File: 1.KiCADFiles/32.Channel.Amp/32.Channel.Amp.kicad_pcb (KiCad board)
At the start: 2 copper layers, 150 x 170.5 mm, 35 parts

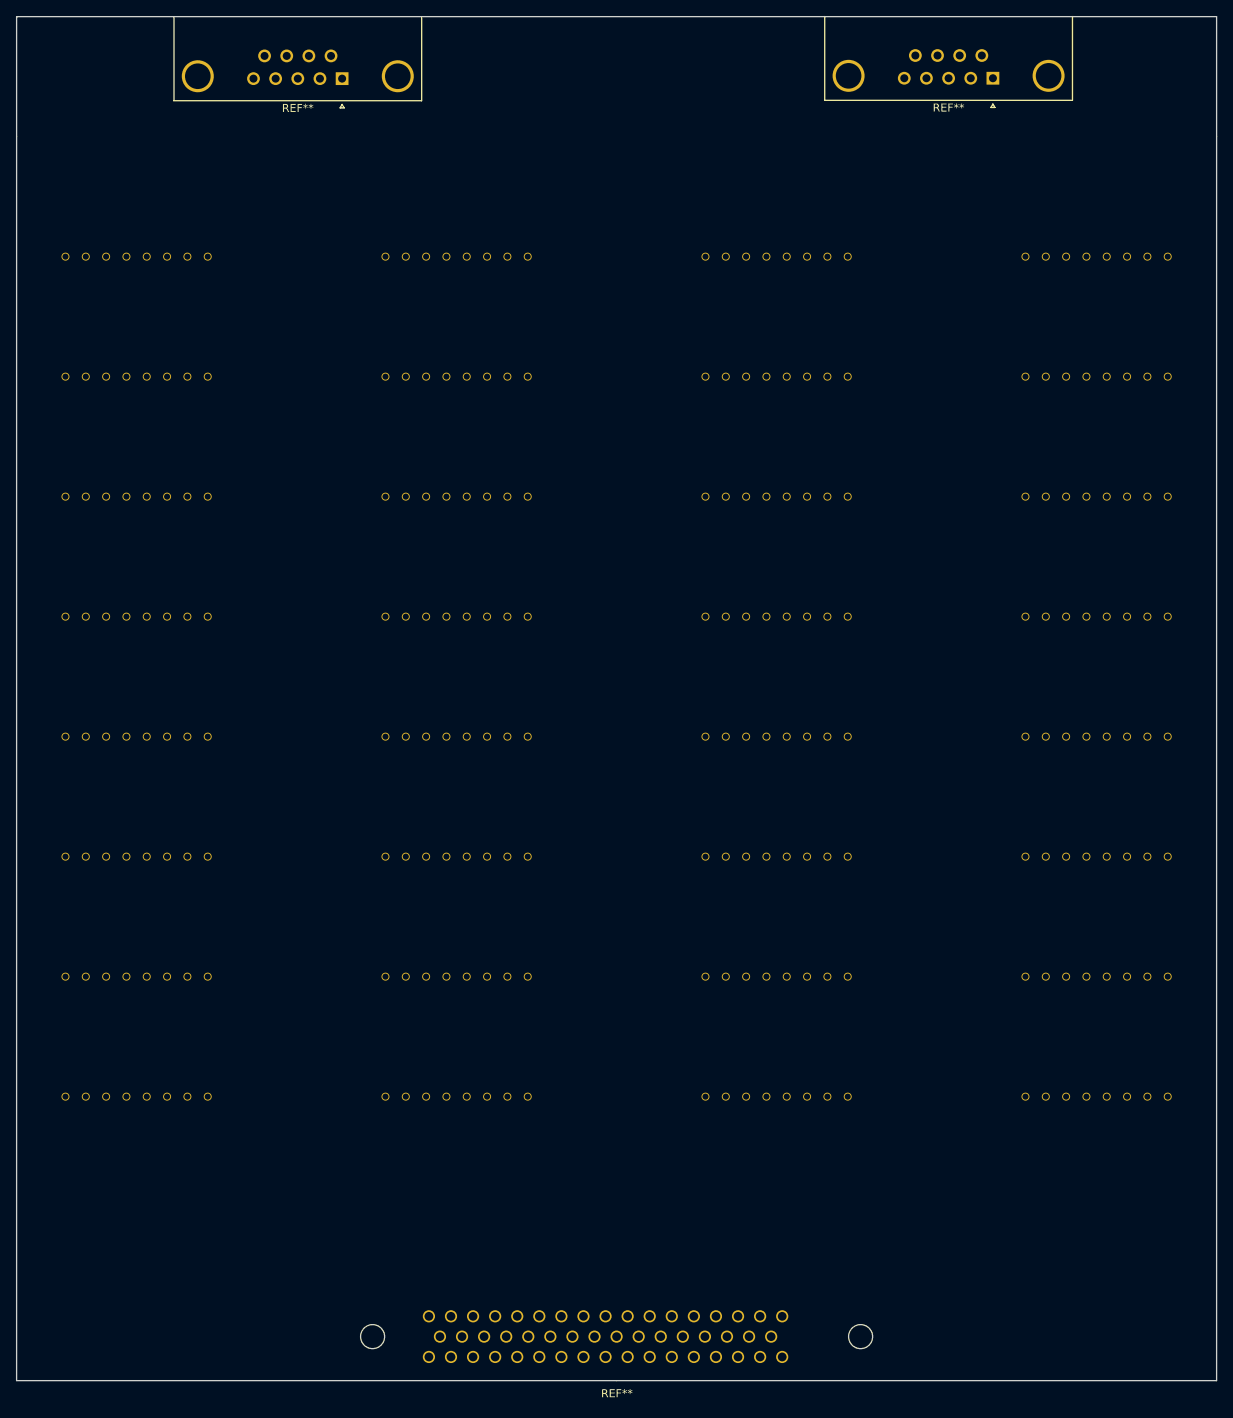
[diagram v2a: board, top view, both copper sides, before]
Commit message: Added +V and -V regulators
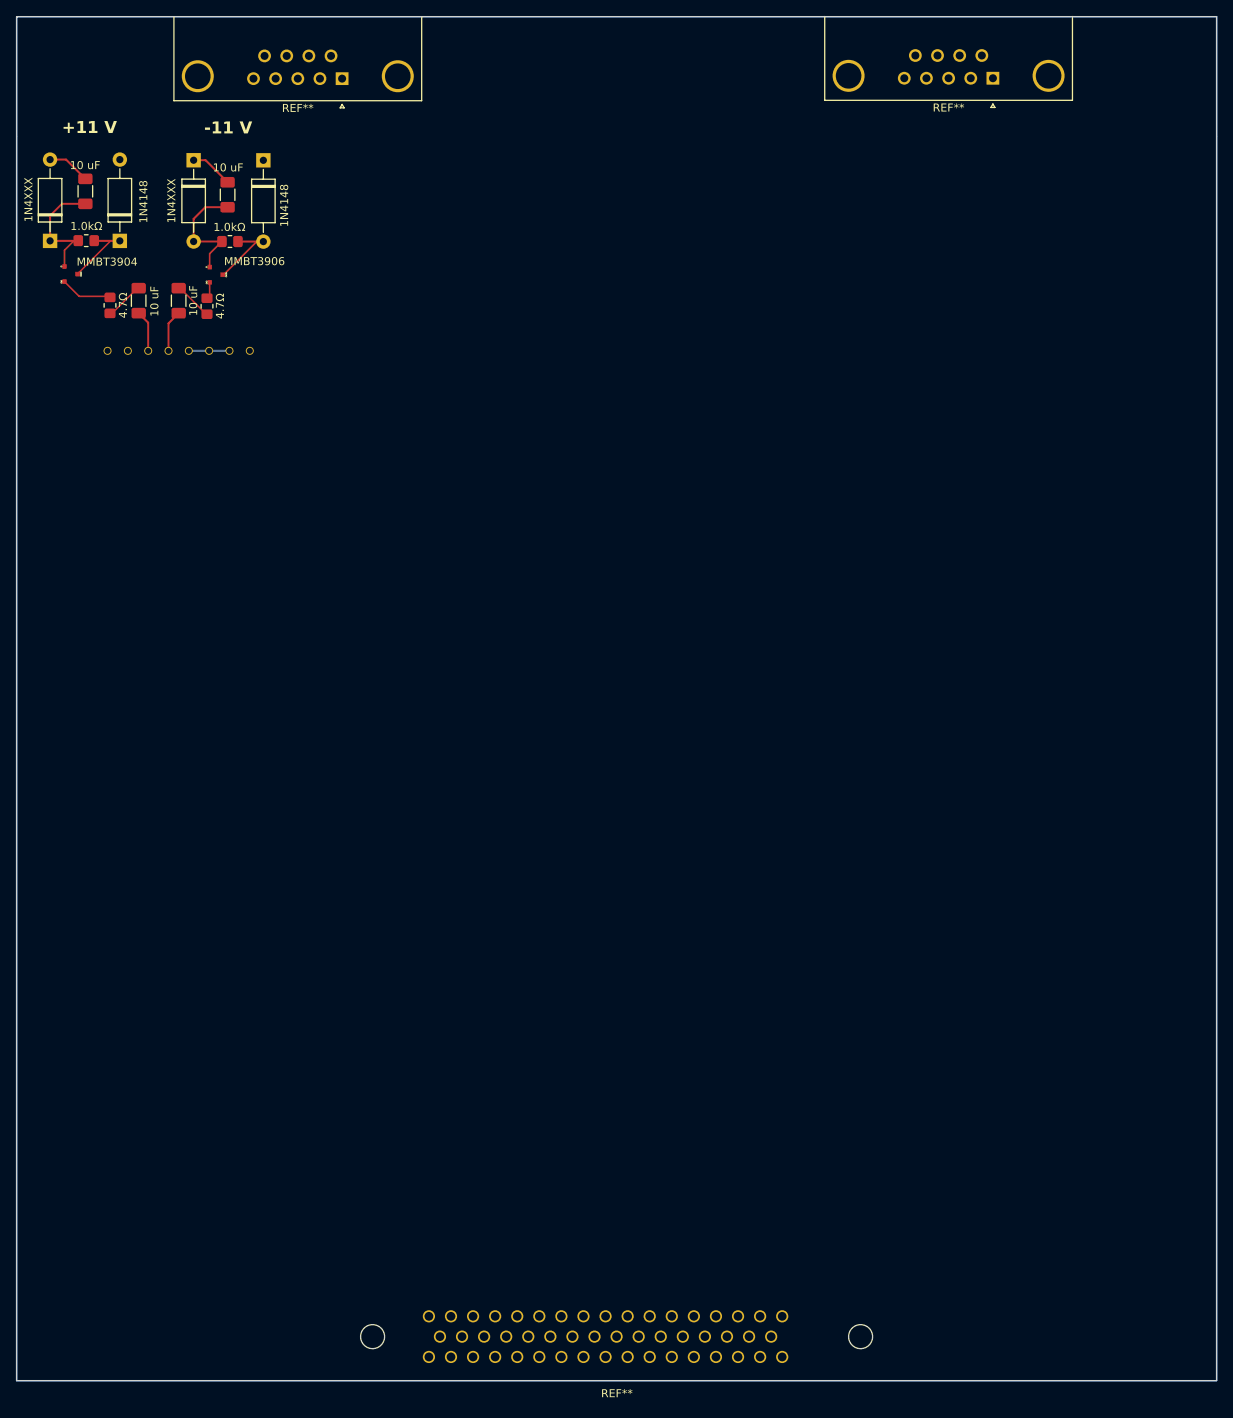
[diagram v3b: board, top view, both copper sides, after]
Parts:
- removed REF**1, REF**10, REF**11, REF**12, REF**13, REF**14, REF**15, REF**16, REF**17, REF**18, REF**19, REF**2, REF**20, REF**21, REF**22, REF**23, REF**24, REF**25, REF**26, REF**27, REF**28, REF**29, REF**3, REF**30, REF**31, REF**4, REF**5, REF**6, REF**7, REF**8, REF**9: SMC-1-08-1-GT, 1.Local.Library:SMC-1-08-1-GT
- added 1.0kΩ: R_0805_2012Metric_Pad1.20x1.40mm_HandSolder, Resistor_SMD:R_0805_2012Metric_Pad1.20x1.40mm_HandSolder, F.Cu at (56.7, 28.1)
- added 1.0kΩ: R_0805_2012Metric_Pad1.20x1.40mm_HandSolder, Resistor_SMD:R_0805_2012Metric_Pad1.20x1.40mm_HandSolder, F.Cu at (38.7, 28.0)
- added 10 uF: C_1206_3216Metric_Pad1.33x1.80mm_HandSolder, Capacitor_SMD:C_1206_3216Metric_Pad1.33x1.80mm_HandSolder, F.Cu at (45.3, 35.5)
- added 10 uF: C_1206_3216Metric_Pad1.33x1.80mm_HandSolder, Capacitor_SMD:C_1206_3216Metric_Pad1.33x1.80mm_HandSolder, F.Cu at (56.4, 22.3)
- added 10 uF: C_1206_3216Metric_Pad1.33x1.80mm_HandSolder, Capacitor_SMD:C_1206_3216Metric_Pad1.33x1.80mm_HandSolder, F.Cu at (50.3, 35.5)
- added 10 uF: C_1206_3216Metric_Pad1.33x1.80mm_HandSolder, Capacitor_SMD:C_1206_3216Metric_Pad1.33x1.80mm_HandSolder, F.Cu at (38.6, 21.8)
- added 1N4148: D_A-405_P10.16mm_Horizontal, Diode_THT:D_A-405_P10.16mm_Horizontal, F.Cu at (60.8, 18.0)
- added 1N4148: D_A-405_P10.16mm_Horizontal, Diode_THT:D_A-405_P10.16mm_Horizontal, F.Cu at (42.9, 28.0)
- added 1N4XXX: D_A-405_P10.16mm_Horizontal, Diode_THT:D_A-405_P10.16mm_Horizontal, F.Cu at (52.1, 17.9)
- added 1N4XXX: D_A-405_P10.16mm_Horizontal, Diode_THT:D_A-405_P10.16mm_Horizontal, F.Cu at (34.2, 28.0)
- added 4.7Ω: R_0805_2012Metric_Pad1.20x1.40mm_HandSolder, Resistor_SMD:R_0805_2012Metric_Pad1.20x1.40mm_HandSolder, F.Cu at (53.8, 36.2)
- added 4.7Ω: R_0805_2012Metric_Pad1.20x1.40mm_HandSolder, Resistor_SMD:R_0805_2012Metric_Pad1.20x1.40mm_HandSolder, F.Cu at (41.7, 36.1)
- added MMBT3904: MMBT3904, 1.Local.Library:MMBT3904, F.Cu at (36.2, 32.2)
- added MMBT3906: MMBT3906, 1.Local.Library:MMBT3906, F.Cu at (54.4, 32.3)
- moved REF** 12.9 mm to (50.3, 41.8), turned to 180 degrees
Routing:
- net (no net): track 0.00 -> 55.8 mm
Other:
- board text added: "+11 V"
- board text added: "-11 V"

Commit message: Added Power Regulator, RC Filtering, and 32 Channel
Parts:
- removed the REF** at (152.0, 7.70)
- added 1.0kΩ: R_0805_2012Metric_Pad1.20x1.40mm_HandSolder, Resistor_SMD:R_0805_2012Metric_Pad1.20x1.40mm_HandSolder, F.Cu at (115.6, 157.9)
- added 1.0kΩ: R_0805_2012Metric_Pad1.20x1.40mm_HandSolder, Resistor_SMD:R_0805_2012Metric_Pad1.20x1.40mm_HandSolder, F.Cu at (93.6, 158.1)
- added 1.0kΩ: R_0805_2012Metric_Pad1.20x1.40mm_HandSolder, Resistor_SMD:R_0805_2012Metric_Pad1.20x1.40mm_HandSolder, F.Cu at (93.6, 118.1)
- added 1.0kΩ: R_0805_2012Metric_Pad1.20x1.40mm_HandSolder, Resistor_SMD:R_0805_2012Metric_Pad1.20x1.40mm_HandSolder, F.Cu at (133.6, 78.1)
- added 1.0kΩ: R_0805_2012Metric_Pad1.20x1.40mm_HandSolder, Resistor_SMD:R_0805_2012Metric_Pad1.20x1.40mm_HandSolder, F.Cu at (155.6, 157.9)
- added 1.0kΩ: R_0805_2012Metric_Pad1.20x1.40mm_HandSolder, Resistor_SMD:R_0805_2012Metric_Pad1.20x1.40mm_HandSolder, F.Cu at (173.6, 118.1)
- added 1.0kΩ: R_0805_2012Metric_Pad1.20x1.40mm_HandSolder, Resistor_SMD:R_0805_2012Metric_Pad1.20x1.40mm_HandSolder, F.Cu at (115.6, 117.9)
- added 1.0kΩ: R_0805_2012Metric_Pad1.20x1.40mm_HandSolder, Resistor_SMD:R_0805_2012Metric_Pad1.20x1.40mm_HandSolder, F.Cu at (75.6, 237.9)
- added 1.0kΩ: R_0805_2012Metric_Pad1.20x1.40mm_HandSolder, Resistor_SMD:R_0805_2012Metric_Pad1.20x1.40mm_HandSolder, F.Cu at (93.6, 278.1)
- added 1.0kΩ: R_0805_2012Metric_Pad1.20x1.40mm_HandSolder, Resistor_SMD:R_0805_2012Metric_Pad1.20x1.40mm_HandSolder, F.Cu at (93.6, 38.1)
- added 1.0kΩ: R_0805_2012Metric_Pad1.20x1.40mm_HandSolder, Resistor_SMD:R_0805_2012Metric_Pad1.20x1.40mm_HandSolder, F.Cu at (155.6, 37.9)
- added 1.0kΩ: R_0805_2012Metric_Pad1.20x1.40mm_HandSolder, Resistor_SMD:R_0805_2012Metric_Pad1.20x1.40mm_HandSolder, F.Cu at (133.6, 198.1)
- added 1.0kΩ: R_0805_2012Metric_Pad1.20x1.40mm_HandSolder, Resistor_SMD:R_0805_2012Metric_Pad1.20x1.40mm_HandSolder, F.Cu at (93.6, 238.1)
- added 1.0kΩ: R_0805_2012Metric_Pad1.20x1.40mm_HandSolder, Resistor_SMD:R_0805_2012Metric_Pad1.20x1.40mm_HandSolder, F.Cu at (173.6, 278.1)
- added 1.0kΩ: R_0805_2012Metric_Pad1.20x1.40mm_HandSolder, Resistor_SMD:R_0805_2012Metric_Pad1.20x1.40mm_HandSolder, F.Cu at (115.6, 237.9)
- added 1.0kΩ: R_0805_2012Metric_Pad1.20x1.40mm_HandSolder, Resistor_SMD:R_0805_2012Metric_Pad1.20x1.40mm_HandSolder, F.Cu at (155.6, 77.9)
- added 1.0kΩ: R_0805_2012Metric_Pad1.20x1.40mm_HandSolder, Resistor_SMD:R_0805_2012Metric_Pad1.20x1.40mm_HandSolder, F.Cu at (173.6, 38.1)
- added 1.0kΩ: R_0805_2012Metric_Pad1.20x1.40mm_HandSolder, Resistor_SMD:R_0805_2012Metric_Pad1.20x1.40mm_HandSolder, F.Cu at (155.6, 117.9)
- added 1.0kΩ: R_0805_2012Metric_Pad1.20x1.40mm_HandSolder, Resistor_SMD:R_0805_2012Metric_Pad1.20x1.40mm_HandSolder, F.Cu at (35.6, 317.9)
- added 1.0kΩ: R_0805_2012Metric_Pad1.20x1.40mm_HandSolder, Resistor_SMD:R_0805_2012Metric_Pad1.20x1.40mm_HandSolder, F.Cu at (133.6, 318.1)
- added 1.0kΩ: R_0805_2012Metric_Pad1.20x1.40mm_HandSolder, Resistor_SMD:R_0805_2012Metric_Pad1.20x1.40mm_HandSolder, F.Cu at (115.6, 77.9)
- added 1.0kΩ: R_0805_2012Metric_Pad1.20x1.40mm_HandSolder, Resistor_SMD:R_0805_2012Metric_Pad1.20x1.40mm_HandSolder, F.Cu at (93.6, 198.1)
- added 1.0kΩ: R_0805_2012Metric_Pad1.20x1.40mm_HandSolder, Resistor_SMD:R_0805_2012Metric_Pad1.20x1.40mm_HandSolder, F.Cu at (35.6, 197.9)
- added 1.0kΩ: R_0805_2012Metric_Pad1.20x1.40mm_HandSolder, Resistor_SMD:R_0805_2012Metric_Pad1.20x1.40mm_HandSolder, F.Cu at (133.6, 238.1)
- added 1.0kΩ: R_0805_2012Metric_Pad1.20x1.40mm_HandSolder, Resistor_SMD:R_0805_2012Metric_Pad1.20x1.40mm_HandSolder, F.Cu at (133.6, 278.1)
- added 1.0kΩ: R_0805_2012Metric_Pad1.20x1.40mm_HandSolder, Resistor_SMD:R_0805_2012Metric_Pad1.20x1.40mm_HandSolder, F.Cu at (53.6, 278.1)
- added 1.0kΩ: R_0805_2012Metric_Pad1.20x1.40mm_HandSolder, Resistor_SMD:R_0805_2012Metric_Pad1.20x1.40mm_HandSolder, F.Cu at (173.6, 78.1)
- added 1.0kΩ: R_0805_2012Metric_Pad1.20x1.40mm_HandSolder, Resistor_SMD:R_0805_2012Metric_Pad1.20x1.40mm_HandSolder, F.Cu at (173.6, 318.1)
- added 1.0kΩ: R_0805_2012Metric_Pad1.20x1.40mm_HandSolder, Resistor_SMD:R_0805_2012Metric_Pad1.20x1.40mm_HandSolder, F.Cu at (35.6, 77.9)
- added 1.0kΩ: R_0805_2012Metric_Pad1.20x1.40mm_HandSolder, Resistor_SMD:R_0805_2012Metric_Pad1.20x1.40mm_HandSolder, F.Cu at (35.6, 117.9)
- added 1.0kΩ: R_0805_2012Metric_Pad1.20x1.40mm_HandSolder, Resistor_SMD:R_0805_2012Metric_Pad1.20x1.40mm_HandSolder, F.Cu at (35.6, 277.9)
- added 1.0kΩ: R_0805_2012Metric_Pad1.20x1.40mm_HandSolder, Resistor_SMD:R_0805_2012Metric_Pad1.20x1.40mm_HandSolder, F.Cu at (75.6, 197.9)
- added 1.0kΩ: R_0805_2012Metric_Pad1.20x1.40mm_HandSolder, Resistor_SMD:R_0805_2012Metric_Pad1.20x1.40mm_HandSolder, F.Cu at (133.6, 38.1)
- added 1.0kΩ: R_0805_2012Metric_Pad1.20x1.40mm_HandSolder, Resistor_SMD:R_0805_2012Metric_Pad1.20x1.40mm_HandSolder, F.Cu at (115.6, 317.9)
- added 1.0kΩ: R_0805_2012Metric_Pad1.20x1.40mm_HandSolder, Resistor_SMD:R_0805_2012Metric_Pad1.20x1.40mm_HandSolder, F.Cu at (53.6, 158.1)
- added 1.0kΩ: R_0805_2012Metric_Pad1.20x1.40mm_HandSolder, Resistor_SMD:R_0805_2012Metric_Pad1.20x1.40mm_HandSolder, F.Cu at (115.6, 277.9)
- added 1.0kΩ: R_0805_2012Metric_Pad1.20x1.40mm_HandSolder, Resistor_SMD:R_0805_2012Metric_Pad1.20x1.40mm_HandSolder, F.Cu at (75.6, 317.9)
- added 1.0kΩ: R_0805_2012Metric_Pad1.20x1.40mm_HandSolder, Resistor_SMD:R_0805_2012Metric_Pad1.20x1.40mm_HandSolder, F.Cu at (53.6, 118.1)
- added 1.0kΩ: R_0805_2012Metric_Pad1.20x1.40mm_HandSolder, Resistor_SMD:R_0805_2012Metric_Pad1.20x1.40mm_HandSolder, F.Cu at (155.6, 237.9)
- added 1.0kΩ: R_0805_2012Metric_Pad1.20x1.40mm_HandSolder, Resistor_SMD:R_0805_2012Metric_Pad1.20x1.40mm_HandSolder, F.Cu at (53.6, 198.1)
- added 1.0kΩ: R_0805_2012Metric_Pad1.20x1.40mm_HandSolder, Resistor_SMD:R_0805_2012Metric_Pad1.20x1.40mm_HandSolder, F.Cu at (155.6, 197.9)
- added 1.0kΩ: R_0805_2012Metric_Pad1.20x1.40mm_HandSolder, Resistor_SMD:R_0805_2012Metric_Pad1.20x1.40mm_HandSolder, F.Cu at (93.6, 78.1)
- added 1.0kΩ: R_0805_2012Metric_Pad1.20x1.40mm_HandSolder, Resistor_SMD:R_0805_2012Metric_Pad1.20x1.40mm_HandSolder, F.Cu at (75.6, 277.9)
- added 1.0kΩ: R_0805_2012Metric_Pad1.20x1.40mm_HandSolder, Resistor_SMD:R_0805_2012Metric_Pad1.20x1.40mm_HandSolder, F.Cu at (35.6, 157.9)
- added 1.0kΩ: R_0805_2012Metric_Pad1.20x1.40mm_HandSolder, Resistor_SMD:R_0805_2012Metric_Pad1.20x1.40mm_HandSolder, F.Cu at (53.6, 78.1)
- added 1.0kΩ: R_0805_2012Metric_Pad1.20x1.40mm_HandSolder, Resistor_SMD:R_0805_2012Metric_Pad1.20x1.40mm_HandSolder, F.Cu at (75.6, 37.9)
- added 1.0kΩ: R_0805_2012Metric_Pad1.20x1.40mm_HandSolder, Resistor_SMD:R_0805_2012Metric_Pad1.20x1.40mm_HandSolder, F.Cu at (53.6, 318.1)
- added 1.0kΩ: R_0805_2012Metric_Pad1.20x1.40mm_HandSolder, Resistor_SMD:R_0805_2012Metric_Pad1.20x1.40mm_HandSolder, F.Cu at (173.6, 238.1)
- added 1.0kΩ: R_0805_2012Metric_Pad1.20x1.40mm_HandSolder, Resistor_SMD:R_0805_2012Metric_Pad1.20x1.40mm_HandSolder, F.Cu at (115.6, 37.9)
- added 1.0kΩ: R_0805_2012Metric_Pad1.20x1.40mm_HandSolder, Resistor_SMD:R_0805_2012Metric_Pad1.20x1.40mm_HandSolder, F.Cu at (53.6, 238.1)
- added 1.0kΩ: R_0805_2012Metric_Pad1.20x1.40mm_HandSolder, Resistor_SMD:R_0805_2012Metric_Pad1.20x1.40mm_HandSolder, F.Cu at (173.6, 198.1)
- added 1.0kΩ: R_0805_2012Metric_Pad1.20x1.40mm_HandSolder, Resistor_SMD:R_0805_2012Metric_Pad1.20x1.40mm_HandSolder, F.Cu at (173.6, 158.1)
- added 1.0kΩ: R_0805_2012Metric_Pad1.20x1.40mm_HandSolder, Resistor_SMD:R_0805_2012Metric_Pad1.20x1.40mm_HandSolder, F.Cu at (155.6, 277.9)
- added 1.0kΩ: R_0805_2012Metric_Pad1.20x1.40mm_HandSolder, Resistor_SMD:R_0805_2012Metric_Pad1.20x1.40mm_HandSolder, F.Cu at (75.6, 157.9)
- added 1.0kΩ: R_0805_2012Metric_Pad1.20x1.40mm_HandSolder, Resistor_SMD:R_0805_2012Metric_Pad1.20x1.40mm_HandSolder, F.Cu at (133.6, 158.1)
- added 1.0kΩ: R_0805_2012Metric_Pad1.20x1.40mm_HandSolder, Resistor_SMD:R_0805_2012Metric_Pad1.20x1.40mm_HandSolder, F.Cu at (75.6, 117.9)
- added 1.0kΩ: R_0805_2012Metric_Pad1.20x1.40mm_HandSolder, Resistor_SMD:R_0805_2012Metric_Pad1.20x1.40mm_HandSolder, F.Cu at (75.6, 77.9)
- added 1.0kΩ: R_0805_2012Metric_Pad1.20x1.40mm_HandSolder, Resistor_SMD:R_0805_2012Metric_Pad1.20x1.40mm_HandSolder, F.Cu at (133.6, 118.1)
- added 1.0kΩ: R_0805_2012Metric_Pad1.20x1.40mm_HandSolder, Resistor_SMD:R_0805_2012Metric_Pad1.20x1.40mm_HandSolder, F.Cu at (115.6, 197.9)
- added 1.0kΩ: R_0805_2012Metric_Pad1.20x1.40mm_HandSolder, Resistor_SMD:R_0805_2012Metric_Pad1.20x1.40mm_HandSolder, F.Cu at (155.6, 317.9)
- added 1.0kΩ: R_0805_2012Metric_Pad1.20x1.40mm_HandSolder, Resistor_SMD:R_0805_2012Metric_Pad1.20x1.40mm_HandSolder, F.Cu at (35.6, 237.9)
- added 1.0kΩ: R_0805_2012Metric_Pad1.20x1.40mm_HandSolder, Resistor_SMD:R_0805_2012Metric_Pad1.20x1.40mm_HandSolder, F.Cu at (93.6, 318.1)
- added 10 uF: C_1206_3216Metric_Pad1.33x1.80mm_HandSolder, Capacitor_SMD:C_1206_3216Metric_Pad1.33x1.80mm_HandSolder, F.Cu at (53.3, 112.2)
- added 10 uF: C_1206_3216Metric_Pad1.33x1.80mm_HandSolder, Capacitor_SMD:C_1206_3216Metric_Pad1.33x1.80mm_HandSolder, F.Cu at (173.3, 112.2)
- added 10 uF: C_1206_3216Metric_Pad1.33x1.80mm_HandSolder, Capacitor_SMD:C_1206_3216Metric_Pad1.33x1.80mm_HandSolder, F.Cu at (155.5, 231.8)
- added 10 uF: C_1206_3216Metric_Pad1.33x1.80mm_HandSolder, Capacitor_SMD:C_1206_3216Metric_Pad1.33x1.80mm_HandSolder, F.Cu at (155.5, 151.8)
- added 10 uF: C_1206_3216Metric_Pad1.33x1.80mm_HandSolder, Capacitor_SMD:C_1206_3216Metric_Pad1.33x1.80mm_HandSolder, F.Cu at (167.2, 85.5)
- added 10 uF: C_1206_3216Metric_Pad1.33x1.80mm_HandSolder, Capacitor_SMD:C_1206_3216Metric_Pad1.33x1.80mm_HandSolder, F.Cu at (127.2, 245.4)
- added 10 uF: C_1206_3216Metric_Pad1.33x1.80mm_HandSolder, Capacitor_SMD:C_1206_3216Metric_Pad1.33x1.80mm_HandSolder, F.Cu at (75.5, 71.8)
- added 10 uF: C_1206_3216Metric_Pad1.33x1.80mm_HandSolder, Capacitor_SMD:C_1206_3216Metric_Pad1.33x1.80mm_HandSolder, F.Cu at (115.5, 271.8)
- added 10 uF: C_1206_3216Metric_Pad1.33x1.80mm_HandSolder, Capacitor_SMD:C_1206_3216Metric_Pad1.33x1.80mm_HandSolder, F.Cu at (173.3, 272.2)
- added 10 uF: C_1206_3216Metric_Pad1.33x1.80mm_HandSolder, Capacitor_SMD:C_1206_3216Metric_Pad1.33x1.80mm_HandSolder, F.Cu at (87.2, 125.5)
- added 10 uF: C_1206_3216Metric_Pad1.33x1.80mm_HandSolder, Capacitor_SMD:C_1206_3216Metric_Pad1.33x1.80mm_HandSolder, F.Cu at (87.2, 45.5)
- added 10 uF: C_1206_3216Metric_Pad1.33x1.80mm_HandSolder, Capacitor_SMD:C_1206_3216Metric_Pad1.33x1.80mm_HandSolder, F.Cu at (42.2, 325.4)
- added 10 uF: C_1206_3216Metric_Pad1.33x1.80mm_HandSolder, Capacitor_SMD:C_1206_3216Metric_Pad1.33x1.80mm_HandSolder, F.Cu at (42.2, 85.5)
- added 10 uF: C_1206_3216Metric_Pad1.33x1.80mm_HandSolder, Capacitor_SMD:C_1206_3216Metric_Pad1.33x1.80mm_HandSolder, F.Cu at (167.2, 45.5)
- added 10 uF: C_1206_3216Metric_Pad1.33x1.80mm_HandSolder, Capacitor_SMD:C_1206_3216Metric_Pad1.33x1.80mm_HandSolder, F.Cu at (53.3, 312.2)
- added 10 uF: C_1206_3216Metric_Pad1.33x1.80mm_HandSolder, Capacitor_SMD:C_1206_3216Metric_Pad1.33x1.80mm_HandSolder, F.Cu at (82.2, 45.5)
- added 10 uF: C_1206_3216Metric_Pad1.33x1.80mm_HandSolder, Capacitor_SMD:C_1206_3216Metric_Pad1.33x1.80mm_HandSolder, F.Cu at (127.2, 85.5)
- added 10 uF: C_1206_3216Metric_Pad1.33x1.80mm_HandSolder, Capacitor_SMD:C_1206_3216Metric_Pad1.33x1.80mm_HandSolder, F.Cu at (35.5, 311.8)
- added 10 uF: C_1206_3216Metric_Pad1.33x1.80mm_HandSolder, Capacitor_SMD:C_1206_3216Metric_Pad1.33x1.80mm_HandSolder, F.Cu at (133.3, 32.2)
- added 10 uF: C_1206_3216Metric_Pad1.33x1.80mm_HandSolder, Capacitor_SMD:C_1206_3216Metric_Pad1.33x1.80mm_HandSolder, F.Cu at (127.2, 45.5)
- added 10 uF: C_1206_3216Metric_Pad1.33x1.80mm_HandSolder, Capacitor_SMD:C_1206_3216Metric_Pad1.33x1.80mm_HandSolder, F.Cu at (122.2, 245.4)
- added 10 uF: C_1206_3216Metric_Pad1.33x1.80mm_HandSolder, Capacitor_SMD:C_1206_3216Metric_Pad1.33x1.80mm_HandSolder, F.Cu at (155.5, 191.8)
- added 10 uF: C_1206_3216Metric_Pad1.33x1.80mm_HandSolder, Capacitor_SMD:C_1206_3216Metric_Pad1.33x1.80mm_HandSolder, F.Cu at (167.2, 325.4)
- added 10 uF: C_1206_3216Metric_Pad1.33x1.80mm_HandSolder, Capacitor_SMD:C_1206_3216Metric_Pad1.33x1.80mm_HandSolder, F.Cu at (35.5, 71.8)
- added 10 uF: C_1206_3216Metric_Pad1.33x1.80mm_HandSolder, Capacitor_SMD:C_1206_3216Metric_Pad1.33x1.80mm_HandSolder, F.Cu at (93.3, 72.2)
- added 10 uF: C_1206_3216Metric_Pad1.33x1.80mm_HandSolder, Capacitor_SMD:C_1206_3216Metric_Pad1.33x1.80mm_HandSolder, F.Cu at (47.2, 245.4)
- added 10 uF: C_1206_3216Metric_Pad1.33x1.80mm_HandSolder, Capacitor_SMD:C_1206_3216Metric_Pad1.33x1.80mm_HandSolder, F.Cu at (133.3, 192.2)
- added 10 uF: C_1206_3216Metric_Pad1.33x1.80mm_HandSolder, Capacitor_SMD:C_1206_3216Metric_Pad1.33x1.80mm_HandSolder, F.Cu at (53.3, 272.2)
- added 10 uF: C_1206_3216Metric_Pad1.33x1.80mm_HandSolder, Capacitor_SMD:C_1206_3216Metric_Pad1.33x1.80mm_HandSolder, F.Cu at (122.2, 45.5)
- added 10 uF: C_1206_3216Metric_Pad1.33x1.80mm_HandSolder, Capacitor_SMD:C_1206_3216Metric_Pad1.33x1.80mm_HandSolder, F.Cu at (53.3, 232.2)
- added 10 uF: C_1206_3216Metric_Pad1.33x1.80mm_HandSolder, Capacitor_SMD:C_1206_3216Metric_Pad1.33x1.80mm_HandSolder, F.Cu at (93.3, 272.2)
- added 10 uF: C_1206_3216Metric_Pad1.33x1.80mm_HandSolder, Capacitor_SMD:C_1206_3216Metric_Pad1.33x1.80mm_HandSolder, F.Cu at (75.5, 311.8)
- added 10 uF: C_1206_3216Metric_Pad1.33x1.80mm_HandSolder, Capacitor_SMD:C_1206_3216Metric_Pad1.33x1.80mm_HandSolder, F.Cu at (93.3, 112.2)
- added 10 uF: C_1206_3216Metric_Pad1.33x1.80mm_HandSolder, Capacitor_SMD:C_1206_3216Metric_Pad1.33x1.80mm_HandSolder, F.Cu at (47.2, 165.4)
- added 10 uF: C_1206_3216Metric_Pad1.33x1.80mm_HandSolder, Capacitor_SMD:C_1206_3216Metric_Pad1.33x1.80mm_HandSolder, F.Cu at (47.2, 205.4)
- added 10 uF: C_1206_3216Metric_Pad1.33x1.80mm_HandSolder, Capacitor_SMD:C_1206_3216Metric_Pad1.33x1.80mm_HandSolder, F.Cu at (167.2, 285.4)
- added 10 uF: C_1206_3216Metric_Pad1.33x1.80mm_HandSolder, Capacitor_SMD:C_1206_3216Metric_Pad1.33x1.80mm_HandSolder, F.Cu at (162.2, 285.4)
- added 10 uF: C_1206_3216Metric_Pad1.33x1.80mm_HandSolder, Capacitor_SMD:C_1206_3216Metric_Pad1.33x1.80mm_HandSolder, F.Cu at (82.2, 245.4)
- added 10 uF: C_1206_3216Metric_Pad1.33x1.80mm_HandSolder, Capacitor_SMD:C_1206_3216Metric_Pad1.33x1.80mm_HandSolder, F.Cu at (173.3, 192.2)
- added 10 uF: C_1206_3216Metric_Pad1.33x1.80mm_HandSolder, Capacitor_SMD:C_1206_3216Metric_Pad1.33x1.80mm_HandSolder, F.Cu at (35.5, 111.8)
- added 10 uF: C_1206_3216Metric_Pad1.33x1.80mm_HandSolder, Capacitor_SMD:C_1206_3216Metric_Pad1.33x1.80mm_HandSolder, F.Cu at (173.3, 152.2)
- added 10 uF: C_1206_3216Metric_Pad1.33x1.80mm_HandSolder, Capacitor_SMD:C_1206_3216Metric_Pad1.33x1.80mm_HandSolder, F.Cu at (75.5, 151.8)
- added 10 uF: C_1206_3216Metric_Pad1.33x1.80mm_HandSolder, Capacitor_SMD:C_1206_3216Metric_Pad1.33x1.80mm_HandSolder, F.Cu at (127.2, 285.4)
- added 10 uF: C_1206_3216Metric_Pad1.33x1.80mm_HandSolder, Capacitor_SMD:C_1206_3216Metric_Pad1.33x1.80mm_HandSolder, F.Cu at (53.3, 152.2)
- added 10 uF: C_1206_3216Metric_Pad1.33x1.80mm_HandSolder, Capacitor_SMD:C_1206_3216Metric_Pad1.33x1.80mm_HandSolder, F.Cu at (87.2, 85.5)
- added 10 uF: C_1206_3216Metric_Pad1.33x1.80mm_HandSolder, Capacitor_SMD:C_1206_3216Metric_Pad1.33x1.80mm_HandSolder, F.Cu at (115.5, 111.8)
- added 10 uF: C_1206_3216Metric_Pad1.33x1.80mm_HandSolder, Capacitor_SMD:C_1206_3216Metric_Pad1.33x1.80mm_HandSolder, F.Cu at (115.5, 31.8)
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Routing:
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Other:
- board size 150 x 170.5 mm -> 163.3 x 360.6 mm

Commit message: Added Single Channel
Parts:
- removed the 1.0kΩ at (115.6, 157.9)
- removed the 1.0kΩ at (93.6, 158.1)
- removed the 1.0kΩ at (93.6, 118.1)
- removed the 1.0kΩ at (133.6, 78.1)
- removed the 1.0kΩ at (155.6, 157.9)
- removed the 1.0kΩ at (173.6, 118.1)
- removed the 1.0kΩ at (115.6, 117.9)
- removed the 1.0kΩ at (75.6, 237.9)
- removed the 1.0kΩ at (93.6, 278.1)
- removed the 1.0kΩ at (93.6, 38.1)
- removed the 1.0kΩ at (155.6, 37.9)
- removed the 1.0kΩ at (133.6, 198.1)
- removed the 1.0kΩ at (93.6, 238.1)
- removed the 1.0kΩ at (173.6, 278.1)
- removed the 1.0kΩ at (115.6, 237.9)
- removed the 1.0kΩ at (155.6, 77.9)
- removed the 1.0kΩ at (173.6, 38.1)
- removed the 1.0kΩ at (155.6, 117.9)
- removed the 1.0kΩ at (35.6, 317.9)
- removed the 1.0kΩ at (133.6, 318.1)
- removed the 1.0kΩ at (115.6, 77.9)
- removed the 1.0kΩ at (93.6, 198.1)
- removed the 1.0kΩ at (35.6, 197.9)
- removed the 1.0kΩ at (133.6, 238.1)
- removed the 1.0kΩ at (133.6, 278.1)
- removed the 1.0kΩ at (53.6, 278.1)
- removed the 1.0kΩ at (173.6, 78.1)
- removed the 1.0kΩ at (173.6, 318.1)
- removed the 1.0kΩ at (35.6, 77.9)
- removed the 1.0kΩ at (35.6, 117.9)
- removed the 1.0kΩ at (35.6, 277.9)
- removed the 1.0kΩ at (75.6, 197.9)
- removed the 1.0kΩ at (133.6, 38.1)
- removed the 1.0kΩ at (115.6, 317.9)
- removed the 1.0kΩ at (53.6, 158.1)
- removed the 1.0kΩ at (115.6, 277.9)
- removed the 1.0kΩ at (75.6, 317.9)
- removed the 1.0kΩ at (53.6, 118.1)
- removed the 1.0kΩ at (155.6, 237.9)
- removed the 1.0kΩ at (53.6, 198.1)
- removed the 1.0kΩ at (155.6, 197.9)
- removed the 1.0kΩ at (93.6, 78.1)
- removed the 1.0kΩ at (75.6, 277.9)
- removed the 1.0kΩ at (35.6, 157.9)
- removed the 1.0kΩ at (53.6, 78.1)
- removed the 1.0kΩ at (75.6, 37.9)
- removed the 1.0kΩ at (53.6, 318.1)
- removed the 1.0kΩ at (173.6, 238.1)
- removed the 1.0kΩ at (115.6, 37.9)
- removed the 1.0kΩ at (53.6, 238.1)
- removed the 1.0kΩ at (173.6, 198.1)
- removed the 1.0kΩ at (173.6, 158.1)
- removed the 1.0kΩ at (155.6, 277.9)
- removed the 1.0kΩ at (75.6, 157.9)
- removed the 1.0kΩ at (133.6, 158.1)
- removed the 1.0kΩ at (75.6, 117.9)
- removed the 1.0kΩ at (75.6, 77.9)
- removed the 1.0kΩ at (133.6, 118.1)
- removed the 1.0kΩ at (115.6, 197.9)
- removed the 1.0kΩ at (155.6, 317.9)
- removed the 1.0kΩ at (35.6, 237.9)
- removed the 1.0kΩ at (93.6, 318.1)
- removed the 10 uF at (53.3, 112.2)
- removed the 10 uF at (173.3, 112.2)
- removed the 10 uF at (155.5, 231.8)
- removed the 10 uF at (155.5, 151.8)
- removed the 10 uF at (167.2, 85.5)
- removed the 10 uF at (127.2, 245.4)
- removed the 10 uF at (75.5, 71.8)
- removed the 10 uF at (115.5, 271.8)
- removed the 10 uF at (173.3, 272.2)
- removed the 10 uF at (87.2, 125.5)
- removed the 10 uF at (87.2, 45.5)
- removed the 10 uF at (42.2, 325.4)
- removed the 10 uF at (42.2, 85.5)
- removed the 10 uF at (167.2, 45.5)
- removed the 10 uF at (53.3, 312.2)
- removed the 10 uF at (82.2, 45.5)
- removed the 10 uF at (127.2, 85.5)
- removed the 10 uF at (35.5, 311.8)
- removed the 10 uF at (133.3, 32.2)
- removed the 10 uF at (127.2, 45.5)
- removed the 10 uF at (122.2, 245.4)
- removed the 10 uF at (155.5, 191.8)
- removed the 10 uF at (167.2, 325.4)
- removed the 10 uF at (35.5, 71.8)
- removed the 10 uF at (93.3, 72.2)
- removed the 10 uF at (47.2, 245.4)
- removed the 10 uF at (133.3, 192.2)
- removed the 10 uF at (53.3, 272.2)
- removed the 10 uF at (122.2, 45.5)
- removed the 10 uF at (53.3, 232.2)
- removed the 10 uF at (93.3, 272.2)
- removed the 10 uF at (75.5, 311.8)
- removed the 10 uF at (93.3, 112.2)
- removed the 10 uF at (47.2, 165.4)
- removed the 10 uF at (47.2, 205.4)
- removed the 10 uF at (167.2, 285.4)
- removed the 10 uF at (162.2, 285.4)
- removed the 10 uF at (82.2, 245.4)
- removed the 10 uF at (173.3, 192.2)
- removed the 10 uF at (35.5, 111.8)
- removed the 10 uF at (173.3, 152.2)
- removed the 10 uF at (75.5, 151.8)
- removed the 10 uF at (127.2, 285.4)
- removed the 10 uF at (53.3, 152.2)
- removed the 10 uF at (87.2, 85.5)
- removed the 10 uF at (115.5, 111.8)
- removed the 10 uF at (115.5, 31.8)
- removed the 10 uF at (167.2, 125.5)
- removed the 10 uF at (122.2, 325.4)
- removed the 10 uF at (122.2, 285.4)
- removed the 10 uF at (173.3, 32.2)
- removed the 10 uF at (122.2, 165.4)
- removed the 10 uF at (47.2, 125.5)
- removed the 10 uF at (82.2, 205.4)
- removed the 10 uF at (127.2, 165.4)
- removed the 10 uF at (75.5, 271.8)
- removed the 10 uF at (167.2, 165.4)
- removed the 10 uF at (162.2, 125.5)
- removed the 10 uF at (47.2, 285.4)
- removed the 10 uF at (35.5, 271.8)
- removed the 10 uF at (115.5, 191.8)
- removed the 10 uF at (127.2, 125.5)
- removed the 10 uF at (133.3, 312.2)
- removed the 10 uF at (42.2, 205.4)
- removed the 10 uF at (155.5, 271.8)
- removed the 10 uF at (115.5, 151.8)
- removed the 10 uF at (42.2, 165.4)
- removed the 10 uF at (35.5, 191.8)
- removed the 10 uF at (82.2, 125.5)
- removed the 10 uF at (162.2, 245.4)
- removed the 10 uF at (133.3, 232.2)
- removed the 10 uF at (155.5, 311.8)
- removed the 10 uF at (75.5, 31.8)
- removed the 10 uF at (173.3, 72.2)
- removed the 10 uF at (87.2, 285.4)
- removed the 10 uF at (162.2, 165.4)
- removed the 10 uF at (47.2, 85.5)
- removed the 10 uF at (87.2, 325.4)
- removed the 10 uF at (42.2, 125.5)
- removed the 10 uF at (133.3, 272.2)
- removed the 10 uF at (115.5, 311.8)
- removed the 10 uF at (93.3, 192.2)
- removed the 10 uF at (155.5, 31.8)
- removed the 10 uF at (127.2, 205.4)
- removed the 10 uF at (115.5, 71.8)
- removed the 10 uF at (122.2, 125.5)
- removed the 10 uF at (162.2, 45.5)
- removed the 10 uF at (133.3, 112.2)
- removed the 10 uF at (93.3, 232.2)
- removed the 10 uF at (82.2, 85.5)
- removed the 10 uF at (115.5, 231.8)
- removed the 10 uF at (173.3, 232.2)
- removed the 10 uF at (75.5, 191.8)
- removed the 10 uF at (53.3, 72.2)
- removed the 10 uF at (162.2, 205.4)
- removed the 10 uF at (162.2, 85.5)
- removed the 10 uF at (35.5, 151.8)
- removed the 10 uF at (87.2, 205.4)
- removed the 10 uF at (42.2, 245.4)
- removed the 10 uF at (82.2, 165.4)
- removed the 10 uF at (167.2, 245.4)
- removed the 10 uF at (155.5, 111.8)
- removed the 10 uF at (133.3, 152.2)
- removed the 10 uF at (167.2, 205.4)
- removed the 10 uF at (133.3, 72.2)
- removed the 10 uF at (122.2, 205.4)
- removed the 10 uF at (75.5, 231.8)
- removed the 10 uF at (173.3, 312.2)
- removed the 10 uF at (127.2, 325.4)
- removed the 10 uF at (42.2, 285.4)
- removed the 10 uF at (87.2, 165.4)
- removed the 10 uF at (53.3, 192.2)
- removed the 10 uF at (93.3, 32.2)
- removed the 10 uF at (93.3, 152.2)
- removed the 10 uF at (82.2, 325.4)
- removed the 10 uF at (155.5, 71.8)
- removed the 10 uF at (93.3, 312.2)
- removed the 10 uF at (75.5, 111.8)
- removed the 10 uF at (82.2, 285.4)
- removed the 10 uF at (162.2, 325.4)
- removed the 10 uF at (122.2, 85.5)
- removed the 10 uF at (87.2, 245.4)
- removed the 10 uF at (35.5, 231.8)
- removed the 10 uF at (47.2, 325.4)
- removed the 1N4148 at (119.8, 278.0)
- removed the 1N4148 at (177.8, 27.9)
- removed the 1N4148 at (57.8, 107.9)
- removed the 1N4148 at (119.8, 158.0)
- removed the 1N4148 at (159.8, 158.0)
- removed the 1N4148 at (137.8, 107.9)
- removed the 1N4148 at (39.8, 118.0)
- removed the 1N4148 at (159.8, 278.0)
- removed the 1N4148 at (177.8, 267.9)
- removed the 1N4148 at (159.8, 78.0)
- removed the 1N4148 at (97.8, 187.9)
- removed the 1N4148 at (159.8, 318.0)
- removed the 1N4148 at (57.8, 267.9)
- removed the 1N4148 at (137.8, 27.9)
- removed the 1N4148 at (39.8, 318.0)
- removed the 1N4148 at (79.8, 318.0)
- removed the 1N4148 at (137.8, 307.9)
- removed the 1N4148 at (137.8, 187.9)
- removed the 1N4148 at (97.8, 147.9)
- removed the 1N4148 at (177.8, 107.9)
- removed the 1N4148 at (97.8, 267.9)
- removed the 1N4148 at (39.8, 198.0)
- removed the 1N4148 at (119.8, 78.0)
- removed the 1N4148 at (137.8, 227.9)
- removed the 1N4148 at (57.8, 147.9)
- removed the 1N4148 at (177.8, 227.9)
- removed the 1N4148 at (79.8, 158.0)
- removed the 1N4148 at (57.8, 187.9)
- removed the 1N4148 at (79.8, 38.0)
- removed the 1N4148 at (159.8, 198.0)
- removed the 1N4148 at (159.8, 238.0)
- removed the 1N4148 at (119.8, 238.0)
- removed the 1N4148 at (137.8, 67.9)
- removed the 1N4148 at (79.8, 78.0)
- removed the 1N4148 at (159.8, 118.0)
- removed the 1N4148 at (119.8, 318.0)
- removed the 1N4148 at (137.8, 267.9)
- removed the 1N4148 at (39.8, 238.0)
- removed the 1N4148 at (39.8, 278.0)
- removed the 1N4148 at (57.8, 307.9)
- removed the 1N4148 at (97.8, 307.9)
- removed the 1N4148 at (159.8, 38.0)
- removed the 1N4148 at (79.8, 198.0)
- removed the 1N4148 at (39.8, 78.0)
- removed the 1N4148 at (177.8, 307.9)
- removed the 1N4148 at (177.8, 67.9)
- removed the 1N4148 at (79.8, 118.0)
- removed the 1N4148 at (57.8, 227.9)
- removed the 1N4148 at (137.8, 147.9)
- removed the 1N4148 at (39.8, 158.0)
- removed the 1N4148 at (97.8, 27.9)
- removed the 1N4148 at (119.8, 198.0)
- removed the 1N4148 at (177.8, 187.9)
- removed the 1N4148 at (119.8, 38.0)
- removed the 1N4148 at (79.8, 278.0)
- removed the 1N4148 at (79.8, 238.0)
- removed the 1N4148 at (177.8, 147.9)
- removed the 1N4148 at (57.8, 67.9)
- removed the 1N4148 at (119.8, 118.0)
- removed the 1N4148 at (97.8, 227.9)
- removed the 1N4148 at (97.8, 67.9)
- removed the 1N4148 at (97.8, 107.9)
- removed the 1N4XXX at (31.1, 238.0)
- removed the 1N4XXX at (169.0, 67.9)
- removed the 1N4XXX at (49.0, 67.9)
- removed the 1N4XXX at (71.1, 238.0)
- removed the 1N4XXX at (111.1, 158.0)
- removed the 1N4XXX at (89.0, 107.9)
- removed the 1N4XXX at (71.1, 78.0)
- removed the 1N4XXX at (71.1, 198.0)
- removed the 1N4XXX at (49.0, 227.9)
- removed the 1N4XXX at (169.0, 267.9)
- removed the 1N4XXX at (71.1, 118.0)
- removed the 1N4XXX at (151.1, 278.0)
- removed the 1N4XXX at (169.0, 27.9)
- removed the 1N4XXX at (151.1, 78.0)
- removed the 1N4XXX at (151.1, 198.0)
- removed the 1N4XXX at (71.1, 38.0)
- removed the 1N4XXX at (129.0, 67.9)
- removed the 1N4XXX at (49.0, 267.9)
- removed the 1N4XXX at (71.1, 278.0)
- removed the 1N4XXX at (129.0, 227.9)
- removed the 1N4XXX at (31.1, 278.0)
- removed the 1N4XXX at (31.1, 318.0)
- removed the 1N4XXX at (151.1, 118.0)
- removed the 1N4XXX at (169.0, 307.9)
- removed the 1N4XXX at (49.0, 187.9)
- removed the 1N4XXX at (169.0, 227.9)
- removed the 1N4XXX at (151.1, 318.0)
- removed the 1N4XXX at (111.1, 38.0)
- removed the 1N4XXX at (31.1, 198.0)
- removed the 1N4XXX at (111.1, 238.0)
- removed the 1N4XXX at (89.0, 147.9)
- removed the 1N4XXX at (89.0, 227.9)
- removed the 1N4XXX at (89.0, 267.9)
- removed the 1N4XXX at (49.0, 307.9)
- removed the 1N4XXX at (31.1, 158.0)
- removed the 1N4XXX at (111.1, 118.0)
- removed the 1N4XXX at (31.1, 118.0)
- removed the 1N4XXX at (111.1, 78.0)
- removed the 1N4XXX at (111.1, 278.0)
- removed the 1N4XXX at (151.1, 158.0)
- removed the 1N4XXX at (89.0, 187.9)
- removed the 1N4XXX at (49.0, 107.9)
- removed the 1N4XXX at (169.0, 147.9)
- removed the 1N4XXX at (129.0, 107.9)
- removed the 1N4XXX at (111.1, 318.0)
- removed the 1N4XXX at (169.0, 187.9)
- removed the 1N4XXX at (151.1, 238.0)
- removed the 1N4XXX at (129.0, 307.9)
- removed the 1N4XXX at (71.1, 318.0)
- removed the 1N4XXX at (71.1, 158.0)
- removed the 1N4XXX at (89.0, 307.9)
- removed the 1N4XXX at (111.1, 198.0)
- removed the 1N4XXX at (169.0, 107.9)
- removed the 1N4XXX at (31.1, 78.0)
- removed the 1N4XXX at (129.0, 27.9)
- removed the 1N4XXX at (151.1, 38.0)
- removed the 1N4XXX at (89.0, 27.9)
- removed the 1N4XXX at (129.0, 267.9)
- removed the 1N4XXX at (129.0, 187.9)
- removed the 1N4XXX at (89.0, 67.9)
- removed the 1N4XXX at (129.0, 147.9)
- removed the 1N4XXX at (49.0, 147.9)
- removed the 4.7Ω at (118.6, 166.0)
- removed the 4.7Ω at (130.7, 46.1)
- removed the 4.7Ω at (38.6, 166.0)
- removed the 4.7Ω at (158.6, 126.0)
- removed the 4.7Ω at (78.6, 246.0)
- removed the 4.7Ω at (78.6, 46.0)
- removed the 4.7Ω at (170.7, 86.1)
- removed the 4.7Ω at (50.7, 126.1)
- removed the 4.7Ω at (38.6, 246.0)
- removed the 4.7Ω at (170.7, 286.1)
- removed the 4.7Ω at (118.6, 126.0)
- removed the 4.7Ω at (78.6, 86.0)
- removed the 4.7Ω at (130.7, 246.1)
- removed the 4.7Ω at (90.7, 326.1)
- removed the 4.7Ω at (38.6, 326.0)
- removed the 4.7Ω at (118.6, 286.0)
- removed the 4.7Ω at (38.6, 86.0)
- removed the 4.7Ω at (38.6, 126.0)
- removed the 4.7Ω at (170.7, 246.1)
- removed the 4.7Ω at (90.7, 166.1)
- removed the 4.7Ω at (118.6, 326.0)
- removed the 4.7Ω at (118.6, 206.0)
- removed the 4.7Ω at (130.7, 86.1)
- removed the 4.7Ω at (90.7, 126.1)
- removed the 4.7Ω at (50.7, 286.1)
- removed the 4.7Ω at (118.6, 46.0)
- removed the 4.7Ω at (50.7, 86.1)
- removed the 4.7Ω at (118.6, 246.0)
- removed the 4.7Ω at (38.6, 206.0)
- removed the 4.7Ω at (118.6, 86.0)
- removed the 4.7Ω at (130.7, 166.1)
- removed the 4.7Ω at (170.7, 206.1)
- removed the 4.7Ω at (90.7, 46.1)
- removed the 4.7Ω at (50.7, 206.1)
- removed the 4.7Ω at (158.6, 206.0)
- removed the 4.7Ω at (38.6, 286.0)
- removed the 4.7Ω at (158.6, 86.0)
- removed the 4.7Ω at (130.7, 286.1)
- removed the 4.7Ω at (78.6, 206.0)
- removed the 4.7Ω at (50.7, 246.1)
- removed the 4.7Ω at (158.6, 286.0)
- removed the 4.7Ω at (170.7, 326.1)
- removed the 4.7Ω at (158.6, 46.0)
- removed the 4.7Ω at (170.7, 166.1)
- removed the 4.7Ω at (78.6, 326.0)
- removed the 4.7Ω at (130.7, 206.1)
- removed the 4.7Ω at (50.7, 166.1)
- removed the 4.7Ω at (130.7, 126.1)
- removed the 4.7Ω at (78.6, 166.0)
- removed the 4.7Ω at (78.6, 286.0)
- removed the 4.7Ω at (158.6, 326.0)
- removed the 4.7Ω at (170.7, 126.1)
- removed the 4.7Ω at (130.7, 326.1)
- removed the 4.7Ω at (170.7, 46.1)
- removed the 4.7Ω at (90.7, 286.1)
- removed the 4.7Ω at (90.7, 246.1)
- removed the 4.7Ω at (78.6, 126.0)
- removed the 4.7Ω at (158.6, 166.0)
- removed the 4.7Ω at (158.6, 246.0)
- removed the 4.7Ω at (90.7, 206.1)
- removed the 4.7Ω at (90.7, 86.1)
- removed the 4.7Ω at (50.7, 326.1)
- removed the MMBT3904 at (73.1, 42.1)
- removed the MMBT3904 at (113.1, 122.1)
- removed the MMBT3904 at (113.1, 82.1)
- removed the MMBT3904 at (33.1, 242.1)
- removed the MMBT3904 at (153.1, 202.1)
- removed the MMBT3904 at (73.1, 122.1)
- removed the MMBT3904 at (153.1, 322.1)
- removed the MMBT3904 at (153.1, 82.1)
- removed the MMBT3904 at (113.1, 282.1)
- removed the MMBT3904 at (113.1, 42.1)
- removed the MMBT3904 at (113.1, 242.1)
- removed the MMBT3904 at (73.1, 322.1)
- removed the MMBT3904 at (153.1, 122.1)
- removed the MMBT3904 at (153.1, 242.1)
- removed the MMBT3904 at (33.1, 202.1)
- removed the MMBT3904 at (73.1, 282.1)
- removed the MMBT3904 at (113.1, 322.1)
- removed the MMBT3904 at (153.1, 162.1)
- removed the MMBT3904 at (153.1, 282.1)
- removed the MMBT3904 at (113.1, 202.1)
- removed the MMBT3904 at (33.1, 322.1)
- removed the MMBT3904 at (33.1, 122.1)
- removed the MMBT3904 at (73.1, 202.1)
- removed the MMBT3904 at (33.1, 282.1)
- removed the MMBT3904 at (153.1, 42.1)
- removed the MMBT3904 at (73.1, 162.1)
- removed the MMBT3904 at (33.1, 162.1)
- removed the MMBT3904 at (73.1, 82.1)
- removed the MMBT3904 at (73.1, 242.1)
- removed the MMBT3904 at (113.1, 162.1)
- removed the MMBT3904 at (33.1, 82.1)
- removed the MMBT3906 at (131.3, 42.2)
- removed the MMBT3906 at (91.3, 122.2)
- removed the MMBT3906 at (171.3, 242.2)
- removed the MMBT3906 at (91.3, 322.2)
- removed the MMBT3906 at (171.3, 202.2)
- removed the MMBT3906 at (171.3, 42.2)
- removed the MMBT3906 at (171.3, 282.2)
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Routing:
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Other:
- board size 163.3 x 360.6 mm -> 64 x 3 mm

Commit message: Minor Updates
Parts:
- removed 1.0kΩ (x2), 4.7Ω (x2): R_0805_2012Metric_Pad1.20x1.40mm_HandSolder, Resistor_SMD:R_0805_2012Metric_Pad1.20x1.40mm_HandSolder
- removed 10 uF: C_1206_3216Metric_Pad1.33x1.80mm_HandSolder, Capacitor_SMD:C_1206_3216Metric_Pad1.33x1.80mm_HandSolder (x4)
- removed 1N4148 (x2), 1N4XXX (x2): D_A-405_P10.16mm_Horizontal, Diode_THT:D_A-405_P10.16mm_Horizontal
- removed MMBT3904: MMBT3904, 1.Local.Library:MMBT3904
- removed MMBT3906: MMBT3906, 1.Local.Library:MMBT3906
- removed the REF** at (173.2, 77.4)
- removed the REF** at (175.8, 74.3)
- removed the REF** at (158.0, 80.2)
- removed the REF** at (178.3, 76.4)
- removed the REF** at (165.6, 76.3)
- removed the REF** at (147.8, 82.2)
- removed the REF** at (145.3, 80.2)
- removed the REF** at (180.8, 73.3)
- removed the REF** at (152.9, 81.2)
- removed the REF** at (210.4, 136.5)
- removed the REF** at (163.1, 79.3)
- removed the REF** at (168.1, 78.3)
- removed the REF** at (183.4, 75.4)
- removed the REF** at (160.5, 77.2)
- removed the REF** at (170.7, 75.3)
- removed the REF** at (150.4, 79.2)
- removed the REF** at (155.4, 78.2)
- removed the REF** at (63.9, 107.3)
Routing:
- net (no net): track 43.8 -> 0.00 mm
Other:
- board text removed: "+11 V"
- board text removed: "-11 V"
